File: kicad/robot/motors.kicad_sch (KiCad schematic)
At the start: 15 parts, among them J3 67996-412HLF, U10 SN74AHC125RGYR, U8 Motor1, U9 Motor2

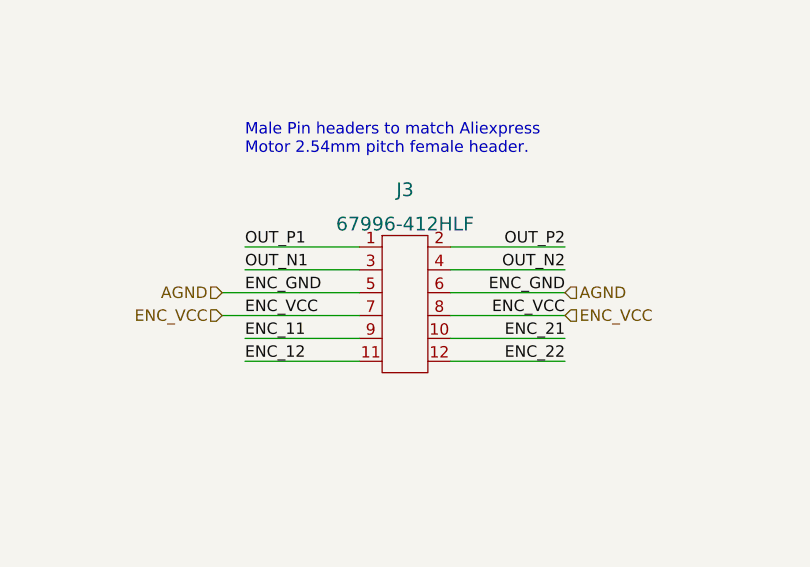
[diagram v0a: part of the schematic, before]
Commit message: Removed conflicting net names on ENC_GND by replacing with text label
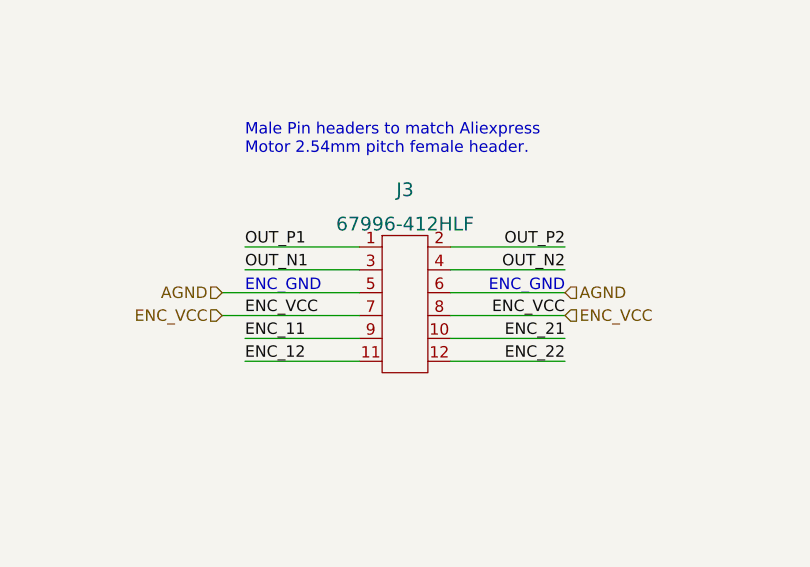
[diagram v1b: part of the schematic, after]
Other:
- note added: "ENC_GND"
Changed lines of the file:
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@@
     (effects (font (size 1.27 1.27)) (justify left bottom))
+  )
+  (text "ENC_GND" (at 255.27 55.88 180)
+    (effects (font (size 1.27 1.27)) (justify right bottom))
   )
   (text "For unidirectional downtranslation \nusing buffer with overvoltage-tolerant inputs\nThis can tolerate up to 7V, but will\nclamp at VCC (3V3) on the outputs."
@@
   )
   (text "Cap to be as close \nto pin 14 (VCC) \nas possible" (at 264.16 163.83 0)
+    (effects (font (size 1.27 1.27)) (justify left bottom))
+  )
+  (text "ENC_GND" (at 219.71 55.88 0)
     (effects (font (size 1.27 1.27)) (justify left bottom))
   )
@@
     (effects (font (size 1.27 1.27)) (justify right bottom))
   )
-  (label "ENC_GND" (at 255.27 55.88 180)
-    (effects (font (size 1.27 1.27)) (justify right bottom))
-  )
   (label "OUT_N2" (at 124.46 137.16 180)
     (effects (font (size 1.27 1.27)) (justify right bottom))
   )
-  (label "ENC_GND" (at 219.71 55.88 0)
-    (effects (font (size 1.27 1.27)) (justify left bottom))
-  )
   (label "ENC_VCC" (at 219.71 58.42 0)

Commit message: Assigned resistor footprints
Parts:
- R26, R27, R28, R29, R30, R31: footprint (none) -> Resistor_SMD:R_0603_1608Metric
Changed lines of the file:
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@@
       (effects (font (size 1.27 1.27)) (justify left))
     )
-    (property "Footprint" "" (id 2) (at 57.912 140.97 90)
+    (property "Footprint" "Resistor_SMD:R_0603_1608Metric" (id 2) (at 57.912 140.97 90)
       (effects (font (size 1.27 1.27)) hide)
     )
@@
       (effects (font (size 1.27 1.27)) (justify left))
     )
-    (property "Footprint" "" (id 2) (at 65.532 41.91 90)
+    (property "Footprint" "Resistor_SMD:R_0603_1608Metric" (id 2) (at 65.532 41.91 90)
       (effects (font (size 1.27 1.27)) hide)
     )
@@
       (effects (font (size 1.27 1.27)) (justify left))
     )
-    (property "Footprint" "" (id 2) (at 57.912 69.85 90)
+    (property "Footprint" "Resistor_SMD:R_0603_1608Metric" (id 2) (at 57.912 69.85 90)
       (effects (font (size 1.27 1.27)) hide)
     )
@@
       (effects (font (size 1.27 1.27)) (justify left))
     )
-    (property "Footprint" "" (id 2) (at 71.882 111.76 90)
+    (property "Footprint" "Resistor_SMD:R_0603_1608Metric" (id 2) (at 71.882 111.76 90)
       (effects (font (size 1.27 1.27)) hide)
     )
@@
       (effects (font (size 1.27 1.27)) (justify left))
     )
-    (property "Footprint" "" (id 2) (at 66.802 140.97 90)
+    (property "Footprint" "Resistor_SMD:R_0603_1608Metric" (id 2) (at 66.802 140.97 90)
       (effects (font (size 1.27 1.27)) hide)
     )
@@
       (effects (font (size 1.27 1.27)) (justify left))
     )
-    (property "Footprint" "" (id 2) (at 66.802 69.85 90)
-      (effects (font (size 1.27 1.27)) hide)
-    )
+    (property "Footprint" "Resistor_SMD:R_0603_1608Metric" (id 2) (at 66.802 69.85 90)
+      (effects (font (size 1.27 1.27)) hide)
+    )

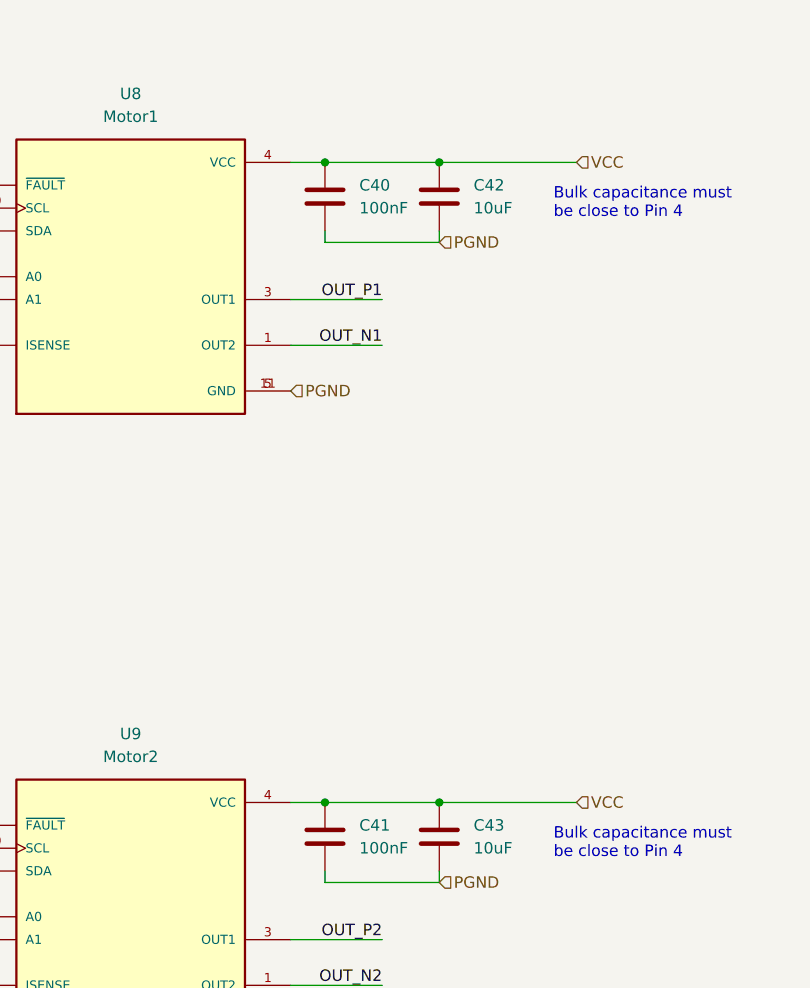
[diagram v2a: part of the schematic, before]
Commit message: Assigned capacitor footprints
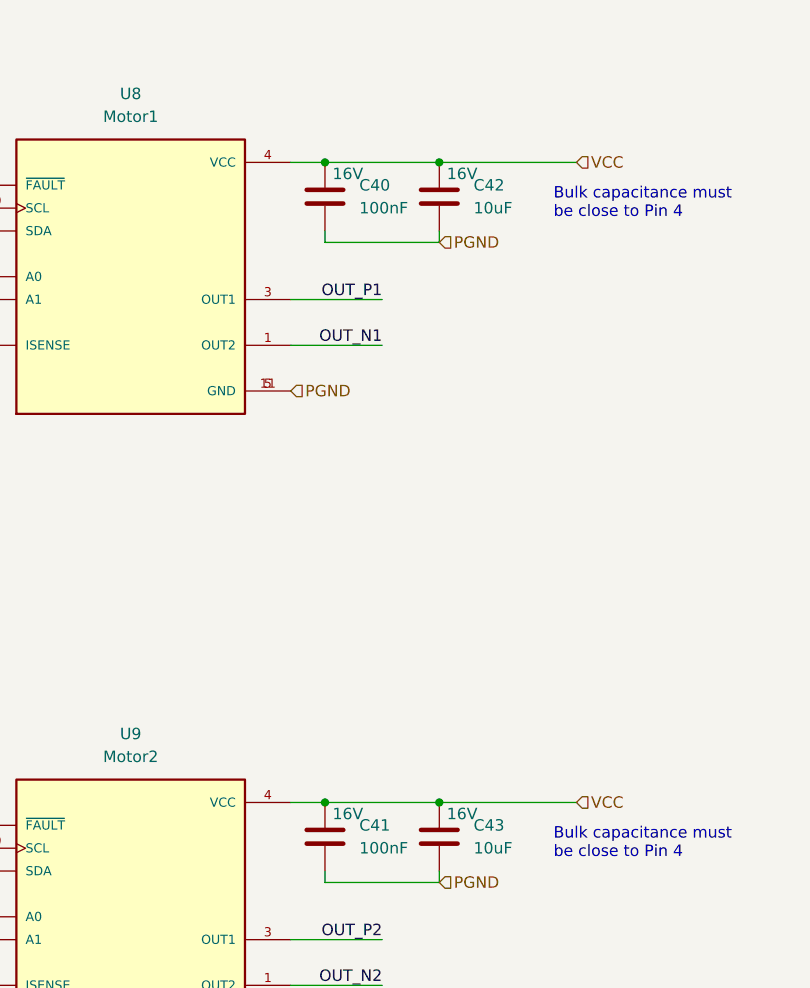
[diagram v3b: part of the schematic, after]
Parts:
- C40, C41, C42, C43: footprint (none) -> Capacitor_SMD:C_0805_2012Metric
- C44: footprint (none) -> Capacitor_SMD:C_0603_1608Metric
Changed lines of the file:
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@@
   )
   (symbol (lib_id "Device:C") (at 130.81 49.53 0) (unit 1)
-    (in_bom yes) (on_board yes) (fields_autoplaced)
+    (in_bom yes) (on_board yes)
     (property "Reference" "C42" (id 0) (at 134.62 48.2599 0)
       (effects (font (size 1.27 1.27)) (justify left))
@@
       (effects (font (size 1.27 1.27)) (justify left))
     )
-    (property "Footprint" "" (id 2) (at 131.7752 53.34 0)
+    (property "Footprint" "Capacitor_SMD:C_0805_2012Metric" (id 2) (at 131.7752 53.34 0)
       (effects (font (size 1.27 1.27)) hide)
     )
@@
       (effects (font (size 1.27 1.27)) hide)
     )
+    (property "Description" "16V" (id 4) (at 133.35 46.99 0))
     (pin "1")
     (pin "2")
@@
   )
   (symbol (lib_id "Device:C") (at 118.11 49.53 0) (unit 1)
-    (in_bom yes) (on_board yes) (fields_autoplaced)
+    (in_bom yes) (on_board yes)
     (property "Reference" "C40" (id 0) (at 121.92 48.2599 0)
       (effects (font (size 1.27 1.27)) (justify left))
@@
       (effects (font (size 1.27 1.27)) (justify left))
     )
-    (property "Footprint" "" (id 2) (at 119.0752 53.34 0)
+    (property "Footprint" "Capacitor_SMD:C_0805_2012Metric" (id 2) (at 119.0752 53.34 0)
       (effects (font (size 1.27 1.27)) hide)
     )
@@
       (effects (font (size 1.27 1.27)) hide)
     )
+    (property "Description" "16V" (id 4) (at 120.65 46.99 0))
     (pin "1")
     (pin "2")
@@
   )
   (symbol (lib_id "Device:C") (at 130.81 120.65 0) (unit 1)
-    (in_bom yes) (on_board yes) (fields_autoplaced)
+    (in_bom yes) (on_board yes)
     (property "Reference" "C43" (id 0) (at 134.62 119.3799 0)
       (effects (font (size 1.27 1.27)) (justify left))
@@
       (effects (font (size 1.27 1.27)) (justify left))
     )
-    (property "Footprint" "" (id 2) (at 131.7752 124.46 0)
+    (property "Footprint" "Capacitor_SMD:C_0805_2012Metric" (id 2) (at 131.7752 124.46 0)
       (effects (font (size 1.27 1.27)) hide)
     )
@@
       (effects (font (size 1.27 1.27)) hide)
     )
+    (property "Description" "16V" (id 4) (at 133.35 118.11 0))
     (pin "1")
     (pin "2")
@@
   )
   (symbol (lib_id "Device:C") (at 118.11 120.65 0) (unit 1)
-    (in_bom yes) (on_board yes) (fields_autoplaced)
+    (in_bom yes) (on_board yes)
     (property "Reference" "C41" (id 0) (at 121.92 119.3799 0)
       (effects (font (size 1.27 1.27)) (justify left))
@@
       (effects (font (size 1.27 1.27)) (justify left))
     )
-    (property "Footprint" "" (id 2) (at 119.0752 124.46 0)
+    (property "Footprint" "Capacitor_SMD:C_0805_2012Metric" (id 2) (at 119.0752 124.46 0)
       (effects (font (size 1.27 1.27)) hide)
     )
@@
       (effects (font (size 1.27 1.27)) hide)
     )
+    (property "Description" "16V" (id 4) (at 120.65 118.11 0))
     (pin "1")
     (pin "2")
@@
       (effects (font (size 1.27 1.27)) (justify left))
     )
-    (property "Footprint" "" (id 2) (at 252.4252 165.1 0)
-      (effects (font (size 1.27 1.27)) hide)
-    )
+    (property "Footprint" "Capacitor_SMD:C_0603_1608Metric" (id 2) (at 252.4252 165.1 0)
+      (effects (font (size 1.27 1.27)) hide)
+    )

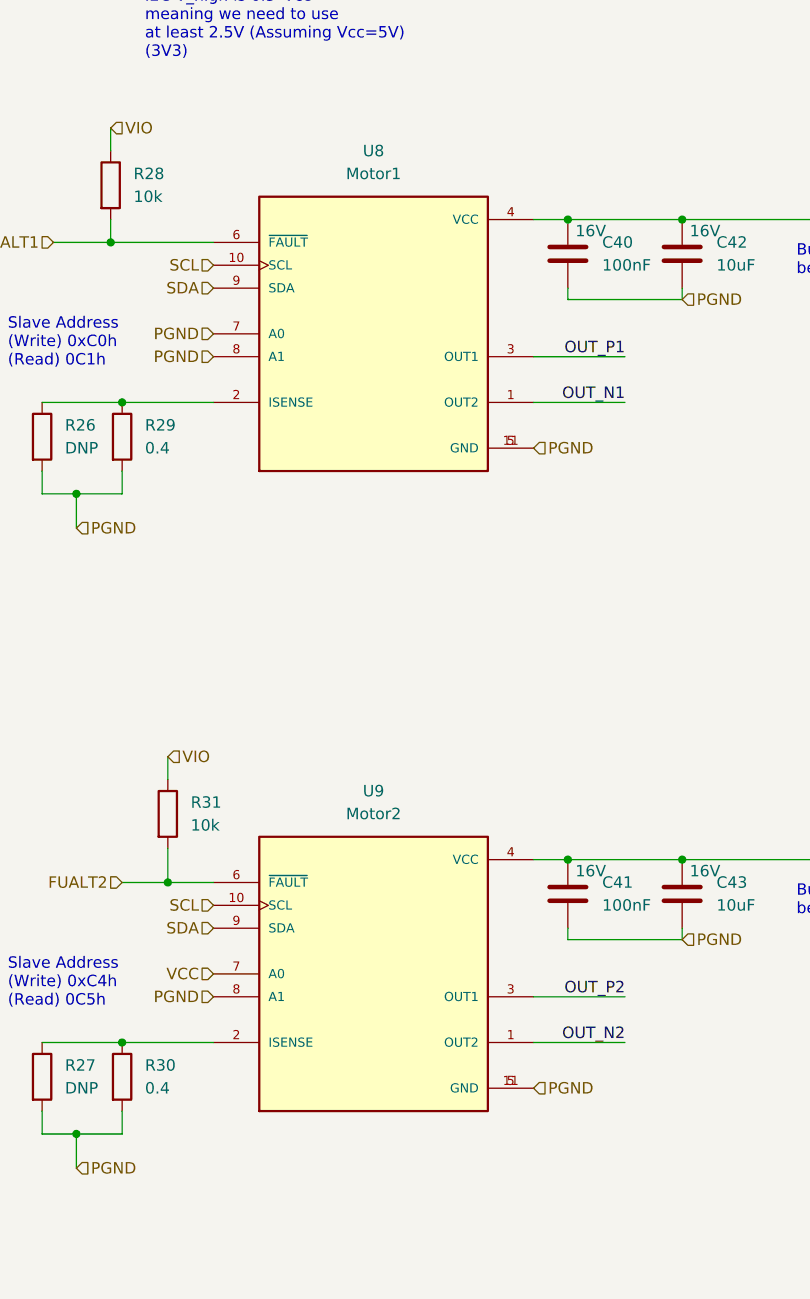
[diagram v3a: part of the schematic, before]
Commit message: Changed values of Motor{1,2} to DRV8830DRCR and added text replacing motor # refs
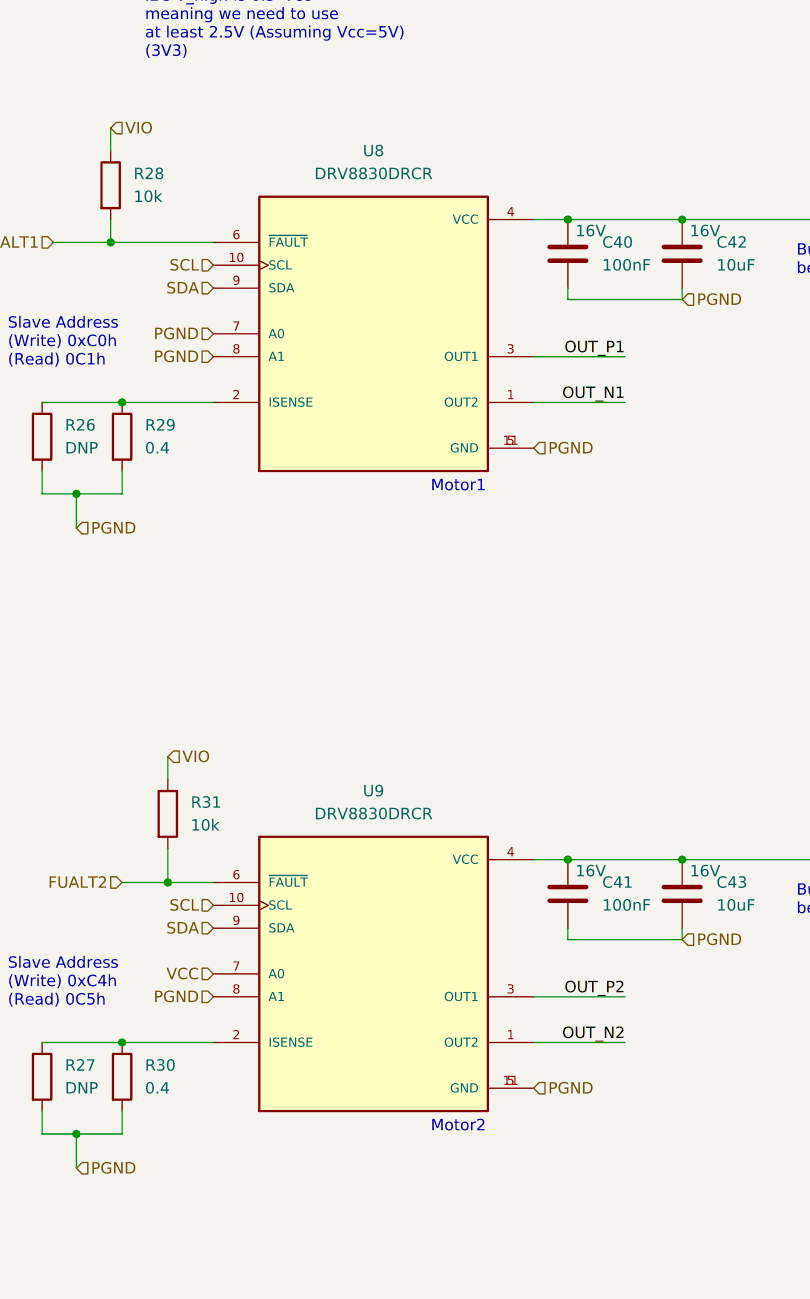
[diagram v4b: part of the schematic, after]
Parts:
- U8: value Motor1 -> DRV8830DRCR
- U9: value Motor2 -> DRV8830DRCR
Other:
- note added: "Motor1"
- note added: "Motor2"
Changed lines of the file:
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@@
     (stroke (width 0) (type default) (color 0 0 0 0))
   )
+  (text "Motor1" (at 102.87 76.2 0)
+    (effects (font (size 1.27 1.27)) (justify left bottom))
+  )
   (text "Bulk capacitance must \nbe close to Pin 4" (at 143.51 123.19 0)
+    (effects (font (size 1.27 1.27)) (justify left bottom))
+  )
+  (text "Motor2" (at 102.87 147.32 0)
     (effects (font (size 1.27 1.27)) (justify left bottom))
   )
@@
     (in_bom yes) (on_board yes) (fields_autoplaced)
     (property "Reference" "U9" (id 0) (at 96.52 109.22 0))
-    (property "Value" "Motor2" (id 1) (at 96.52 111.76 0))
+    (property "Value" "DRV8830DRCR" (id 1) (at 96.52 111.76 0))
     (property "Footprint" "Snapeda:IC_DRV8830DRCR" (id 2) (at 83.82 149.86 0)
       (effects (font (size 1.27 1.27)) (justify left bottom) hide)
@@
     (in_bom yes) (on_board yes) (fields_autoplaced)
     (property "Reference" "U8" (id 0) (at 96.52 38.1 0))
-    (property "Value" "Motor1" (id 1) (at 96.52 40.64 0))
+    (property "Value" "DRV8830DRCR" (id 1) (at 96.52 40.64 0))
     (property "Footprint" "Snapeda:IC_DRV8830DRCR" (id 2) (at 83.82 78.74 0)
       (effects (font (size 1.27 1.27)) (justify left bottom) hide)

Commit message: continue to layut
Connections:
- net OUT_N2: now also J3.2; no longer J3.4
- net OUT_P2: now also J3.4; no longer J3.2
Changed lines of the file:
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@@
     (effects (font (size 1.27 1.27)) (justify right bottom))
   )
-  (label "OUT_N2" (at 255.27 53.34 180)
+  (label "OUT_P2" (at 255.27 53.34 180)
     (effects (font (size 1.27 1.27)) (justify right bottom))
   )
@@
     (effects (font (size 1.27 1.27)) (justify right bottom))
   )
-  (label "OUT_P2" (at 255.27 50.8 180)
+  (label "OUT_N2" (at 255.27 50.8 180)
     (effects (font (size 1.27 1.27)) (justify right bottom))
   )

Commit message: Attached center pad to GND
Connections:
- net AGND: now also U10.PAD (GND)
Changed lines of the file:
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@@
       (effects (font (size 1.524 1.524)) hide)
     )
+    (pin "PAD")
     (pin "1")
     (pin "10")

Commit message: Remove some more DNP parts from BOM
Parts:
- R26, R27: now left out of the parts list
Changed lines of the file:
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@@
   )
   (symbol (lib_id "Device:R") (at 59.69 140.97 0) (unit 1)
-    (in_bom yes) (on_board yes) (fields_autoplaced)
+    (in_bom no) (on_board yes) (fields_autoplaced)
     (property "Reference" "R27" (id 0) (at 62.23 139.6999 0)
       (effects (font (size 1.27 1.27)) (justify left))
@@
   )
   (symbol (lib_id "Device:R") (at 59.69 69.85 0) (unit 1)
-    (in_bom yes) (on_board yes) (fields_autoplaced)
+    (in_bom no) (on_board yes) (fields_autoplaced)
     (property "Reference" "R26" (id 0) (at 62.23 68.5799 0)
       (effects (font (size 1.27 1.27)) (justify left))

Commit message: WARNING Major BOM cleanup
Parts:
- J3: MPN 67996-412HLF -> (none); Part Number (none) -> 67996-412HLF
- U8, U9: MANUFACTURER Texas Instruments -> (none); Manufacturer (none) -> Texas Instruments
- renumbered U10 to Q6
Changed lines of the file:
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@@
   (symbol (lib_id "ultralibrarian:SN74AHC125RGYR") (at 218.44 160.02 0) (unit 1)
     (in_bom yes) (on_board yes) (fields_autoplaced)
-    (property "Reference" "U10" (id 0) (at 221.7294 135.89 0)
+    (property "Reference" "Q6" (id 0) (at 221.7294 135.89 0)
       (effects (font (size 1.524 1.524)) (justify left))
     )
@@
       (effects (font (size 1.27 1.27)) (justify left bottom) hide)
     )
-    (property "MANUFACTURER" "Texas Instruments" (id 6) (at 83.82 152.4 0)
+    (property "MANUFACTURER" "" (id 6) (at 83.82 152.4 0)
       (effects (font (size 1.27 1.27)) (justify left bottom) hide)
     )
@@
     )
     (property "Description" "Provide adequate heat sinking on PCB" (id 8) (at 96.52 129.54 0)
+      (effects (font (size 1.27 1.27)) hide)
+    )
+    (property "Manufacturer" "Texas Instruments" (id 9) (at 96.52 129.54 0)
       (effects (font (size 1.27 1.27)) hide)
     )
@@
       (effects (font (size 1.27 1.27)) (justify left bottom) hide)
     )
-    (property "MANUFACTURER" "Texas Instruments" (id 6) (at 83.82 81.28 0)
+    (property "MANUFACTURER" "" (id 6) (at 83.82 81.28 0)
       (effects (font (size 1.27 1.27)) (justify left bottom) hide)
     )
@@
     )
     (property "Description" "Provide adequate heat sinking on PCB" (id 8) (at 96.52 58.42 0)
+      (effects (font (size 1.27 1.27)) hide)
+    )
+    (property "Manufacturer" "Texas Instruments" (id 9) (at 96.52 58.42 0)
       (effects (font (size 1.27 1.27)) hide)
     )
@@
       (effects (font (size 1.524 1.524)) (justify left) hide)
     )
-    (property "MPN" "67996-412HLF" (id 5) (at 242.57 43.18 0)
+    (property "MPN" "" (id 5) (at 242.57 43.18 0)
       (effects (font (size 1.524 1.524)) (justify left) hide)
     )
@@
       (effects (font (size 1.524 1.524)) (justify left) hide)
     )
-    (pin "1")
+    (property "Part Number" "67996-412HLF" (id 13) (at 237.49 55.88 0)
+      (effects (font (size 1.27 1.27)) hide)
+    )
+    (pin "1")
